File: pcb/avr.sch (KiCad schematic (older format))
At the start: 32 parts, among them IC201 MCU-ATMEGA328P-MU_QFN32_, P201 CONNECTOR, P202 CONNECTOR, P203 CONNECTOR, P204 CONNECTOR, P205 CONNECTOR, P206 CONNECTOR, P207 CONNECTOR, P208 CONNECTOR, P209 CONNECTOR, P210 CONNECTOR, P211 CONNECTOR, P212 CONNECTOR, P213 CONNECTOR, P214 CONNECTOR, P215 CONNECTOR, P216 CONNECTOR, P217 CONNECTOR, P218 CONNECTOR, P219 CONNECTOR, P220 CONNECTOR, P221 CONNECTOR, P222 CONN_01X03, P223 CONNECTOR, P224 CONNECTOR, x201 SMD-CRYSTAL-16MHZ-8PF-20PPM-4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

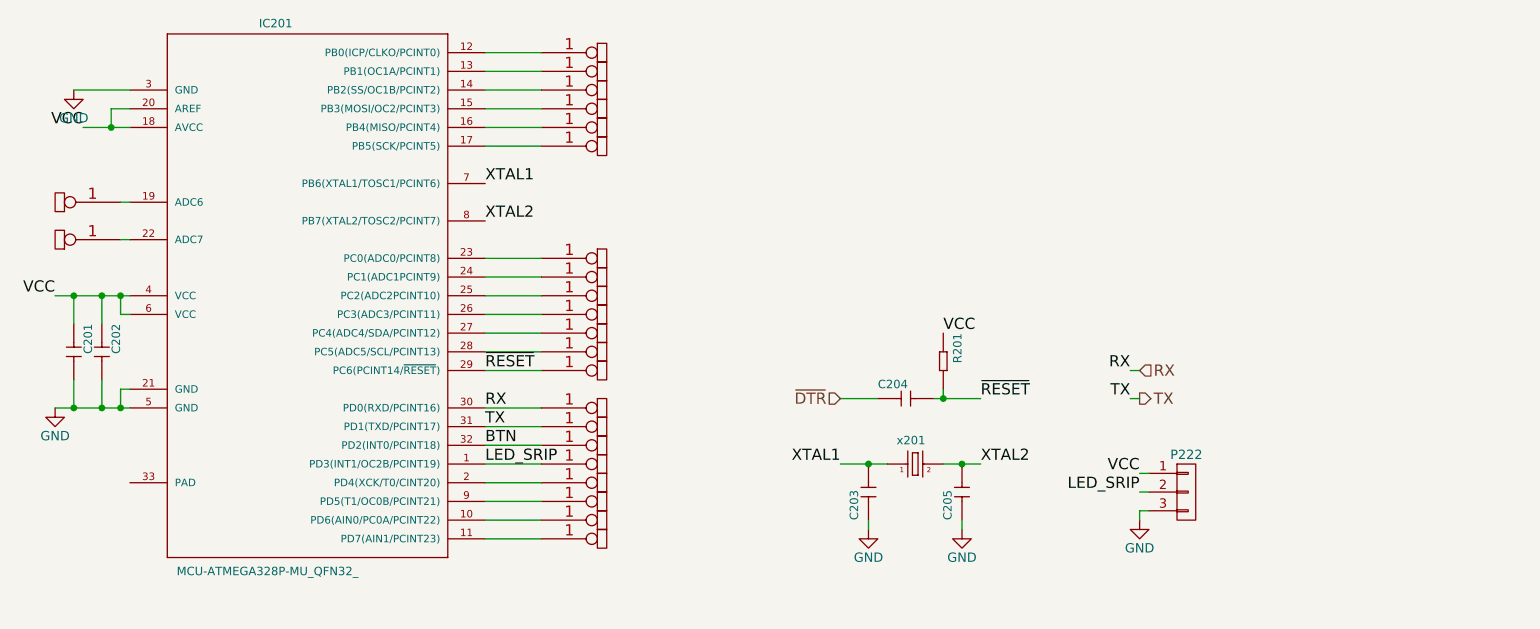
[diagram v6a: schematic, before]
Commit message: added spi header for avr
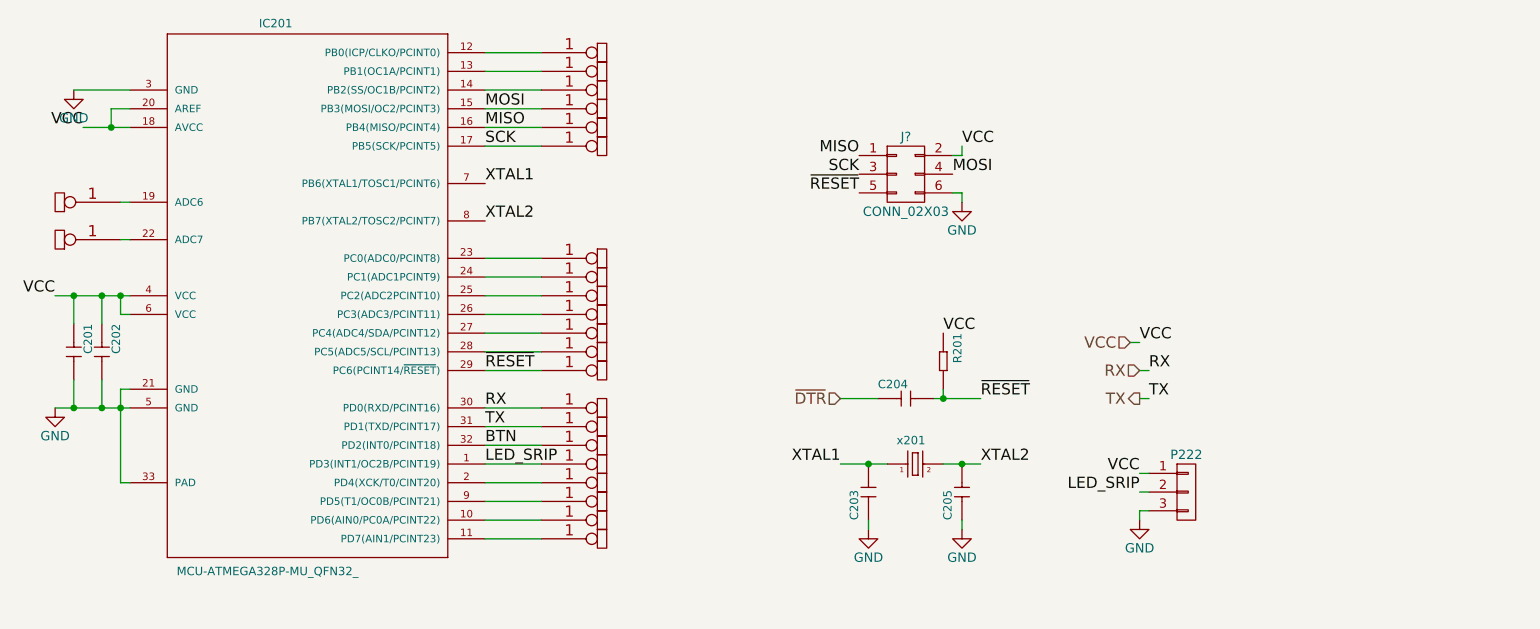
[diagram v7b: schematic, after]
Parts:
- added J?: CONN_02X03, symbol CONN_02X03
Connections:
- net GND: now also IC201.33 (PAD), J?.6 (P6)
- net VCC: now also J?.2 (P2)
- net ~RESET: now also J?.5 (P5)
- net MOSI: now reaches IC201.15 (PB3(MOSI/OC2/PCINT3)), P204.1 (W)
- net MOSI: now also J?.4 (P4)
- net MISO: now reaches IC201.16 (PB4(MISO/PCINT4)), P205.1 (W)
- net MISO: now also J?.1 (P1)
- net SCK: now reaches IC201.17 (PB5(SCK/PCINT5)), P206.1 (W)
- net SCK: now also J?.3 (P3)
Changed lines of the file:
@@
 	1    0    0    -1
 $EndComp
-Wire Wire Line
-	8950 4600 8900 4600
-Wire Wire Line
-	8900 4600 8900 4650
 Text Label 8900 4500 2    60   ~ 0
 LED_SRIP
-Wire Wire Line
-	8950 4500 8900 4500
 Text Label 8900 4400 2    60   ~ 0
 VCC
-Wire Wire Line
-	8950 4400 8900 4400
 $Comp
 L CONNECTOR P223
@@
 	0    1    1    0
 $EndComp
-Wire Wire Line
-	7300 4350 7550 4350
-Wire Wire Line
-	7850 4350 8050 4350
 $Comp
 L GND #PWR09
@@
 	1    0    0    -1
 $EndComp
-Wire Wire Line
-	7450 4650 7450 4700
-Wire Wire Line
-	7950 4650 7950 4700
-Connection ~ 7450 4350
 Text Label 7300 4350 2    60   ~ 0
 XTAL1
 Text Label 8050 4350 0    60   ~ 0
 XTAL2
-Connection ~ 7950 4350
 $Comp
 L CERAMIC-100NF-50V-10%-X7R_0603_ C201
@@
 	1    0    0    -1
 $EndComp
-Wire Wire Line
-	3100 3450 3500 3450
-Wire Wire Line
-	3200 3600 3200 3450
-Connection ~ 3200 3450
-Wire Wire Line
-	3350 3600 3350 3450
-Connection ~ 3350 3450
-Wire Wire Line
-	3500 3550 3450 3550
-Wire Wire Line
-	3450 3550 3450 3450
-Connection ~ 3450 3450
-Wire Wire Line
-	3100 4050 3500 4050
-Wire Wire Line
-	3200 3900 3200 4050
-Connection ~ 3200 4050
-Wire Wire Line
-	3350 3900 3350 4050
-Connection ~ 3350 4050
-Wire Wire Line
-	3500 3950 3450 3950
-Wire Wire Line
-	3450 3950 3450 4050
-Connection ~ 3450 4050
 $Comp
 L GND #PWR012
@@
 Text Label 3250 2550 2    60   ~ 0
 VCC
-Wire Wire Line
-	3250 2550 3500 2550
-Wire Wire Line
-	3500 2350 3200 2350
-Wire Wire Line
-	3500 2450 3400 2450
-Wire Wire Line
-	3400 2450 3400 2550
-Connection ~ 3400 2550
 Text Label 5400 2850 0    60   ~ 0
 XTAL1
 Text Label 5400 3050 0    60   ~ 0
 XTAL2
-Text HLabel 8900 3850 2    60   Input ~ 0
+Text HLabel 8900 3850 0    60   Input ~ 0
 RX
-Text HLabel 8900 4000 2    60   Output ~ 0
+Text HLabel 8900 4000 0    60   Output ~ 0
 TX
-Wire Wire Line
-	5400 4050 5700 4050
-Wire Wire Line
-	5400 4150 5700 4150
 Text Label 5400 4250 0    60   ~ 0
 BTN
@@
 	1    0    0    -1
 $EndComp
-Wire Wire Line
-	7850 3950 7850 4000
-Wire Wire Line
-	7800 4000 8050 4000
-Connection ~ 7850 4000
 Text Label 8050 4000 0    60   ~ 0
 ~RESET
 Text HLabel 7300 4000 0    60   Input ~ 0
 ~DTR
-Wire Wire Line
-	7500 4000 7300 4000
 Text Label 7850 3650 0    60   ~ 0
 VCC
-Wire Wire Line
-	5700 4250 5400 4250
-Wire Wire Line
-	5400 4350 5700 4350
-Wire Wire Line
-	5700 4450 5400 4450
-Wire Wire Line
-	5400 4550 5700 4550
-Wire Wire Line
-	5700 4650 5400 4650
-Wire Wire Line
-	5400 4750 5700 4750
-Wire Wire Line
-	5400 3850 5700 3850
-Wire Wire Line
-	5400 3750 5700 3750
-Wire Wire Line
-	5700 3650 5400 3650
-Wire Wire Line
-	5400 3550 5700 3550
-Wire Wire Line
-	5700 3450 5400 3450
-Wire Wire Line
-	5400 3350 5700 3350
-Wire Wire Line
-	5700 3250 5400 3250
-Wire Wire Line
-	5400 2650 5700 2650
-Wire Wire Line
-	5700 2550 5400 2550
-Wire Wire Line
-	5400 2450 5700 2450
-Wire Wire Line
-	5700 2350 5400 2350
-Wire Wire Line
-	5400 2250 5700 2250
-Wire Wire Line
-	5700 2150 5400 2150
-Wire Wire Line
-	3500 2950 3450 2950
-Wire Wire Line
-	3450 3150 3500 3150
 Text Label 5400 4050 0    60   ~ 0
 RX
 Text Label 5400 4150 0    60   ~ 0
 TX
-Text Label 8850 4000 2    60   ~ 0
+Text Label 8950 4000 0    60   ~ 0
 TX
-Text Label 8850 3850 2    60   ~ 0
+Text Label 8950 3850 0    60   ~ 0
 RX
-Wire Wire Line
-	8900 3850 8850 3850
-Wire Wire Line
-	8900 4000 8850 4000
+$Comp
+L CONN_02X03 J?
+U 1 1 5A551BF4
+P 7650 2800
+F 0 "J?" H 7650 3000 50  0000 C CNN
+F 1 "CONN_02X03" H 7650 2600 50  0000 C CNN
+F 2 "" H 7650 1600 50  0001 C CNN
+F 3 "" H 7650 1600 50  0001 C CNN
+	1    7650 2800
+	1    0    0    -1
+$EndComp
+Text Label 7400 2900 2    60   ~ 0
+~RESET
+Wire Wire Line
+	8950 4600 8900 4600
+Wire Wire Line
+	8900 4600 8900 4650
+Wire Wire Line
+	8950 4500 8900 4500
+Wire Wire Line
+	8950 4400 8900 4400
+Wire Wire Line
+	7300 4350 7450 4350
+Wire Wire Line
+	7450 4350 7550 4350
+Wire Wire Line
+	7850 4350 7950 4350
+Wire Wire Line
+	7950 4350 8050 4350
+Wire Wire Line
+	7450 4650 7450 4700
+Wire Wire Line
+	7950 4650 7950 4700
+Connection ~ 7450 4350
+Connection ~ 7950 4350
+Wire Wire Line
+	3100 3450 3200 3450
+Wire Wire Line
+	3200 3450 3350 3450
+Wire Wire Line
+	3350 3450 3450 3450
+Wire Wire Line
+	3450 3450 3500 3450
+Wire Wire Line
+	3200 3600 3200 3450
+Connection ~ 3200 3450
+Wire Wire Line
+	3350 3600 3350 3450
+Connection ~ 3350 3450
+Wire Wire Line
+	3500 3550 3450 3550
+Wire Wire Line
+	3450 3550 3450 3450
+Connection ~ 3450 3450
+Wire Wire Line
+	3100 4050 3200 4050
+Wire Wire Line
+	3200 4050 3350 4050
+Wire Wire Line
+	3350 4050 3450 4050
+Wire Wire Line
+	3450 4050 3500 4050
+Wire Wire Line
+	3200 3900 3200 4050
+Connection ~ 3200 4050
+Wire Wire Line
+	3350 3900 3350 4050
+Connection ~ 3350 4050
+Wire Wire Line
+	3500 3950 3450 3950
+Wire Wire Line
+	3450 3950 3450 4050
+Wire Wire Line
+	3450 4050 3450 4450
+Connection ~ 3450 4050
+Wire Wire Line
+	3250 2550 3400 2550
+Wire Wire Line
+	3400 2550 3500 2550
+Wire Wire Line
+	3500 2350 3200 2350
+Wire Wire Line
+	3500 2450 3400 2450
+Wire Wire Line
+	3400 2450 3400 2550
+Connection ~ 3400 2550
+Wire Wire Line
+	5400 4050 5700 4050
+Wire Wire Line
+	5400 4150 5700 4150
+Wire Wire Line
+	7850 3950 7850 4000
+Wire Wire Line
+	7800 4000 7850 4000
+Wire Wire Line
+	7850 4000 8050 4000
+Connection ~ 7850 4000
+Wire Wire Line
+	7500 4000 7300 4000
+Wire Wire Line
+	5700 4250 5400 4250
+Wire Wire Line
+	5400 4350 5700 4350
+Wire Wire Line
+	5700 4450 5400 4450
+Wire Wire Line
+	5400 4550 5700 4550
+Wire Wire Line
+	5700 4650 5400 4650
+Wire Wire Line
+	5400 4750 5700 4750
+Wire Wire Line
+	5400 3850 5700 3850
+Wire Wire Line
+	5400 3750 5700 3750
+Wire Wire Line
+	5700 3650 5400 3650
+Wire Wire Line
+	5400 3550 5700 3550
+Wire Wire Line
+	5700 3450 5400 3450
+Wire Wire Line
+	5400 3350 5700 3350
+Wire Wire Line
+	5700 3250 5400 3250
+Wire Wire Line
+	5400 2650 5700 2650
+Wire Wire Line
+	5700 2550 5400 2550
+Wire Wire Line
+	5400 2450 5700 2450
+Wire Wire Line
+	5700 2350 5400 2350
+Wire Wire Line
+	5400 2250 5700 2250
+Wire Wire Line
+	5700 2150 5400 2150
+Wire Wire Line
+	3500 2950 3450 2950
+Wire Wire Line
+	3450 3150 3500 3150
+Wire Wire Line
+	8900 3850 8950 3850
+Wire Wire Line
+	8900 4000 8950 4000
+Wire Wire Line
+	3450 4450 3500 4450
+Text Label 5400 2550 0    60   ~ 0
+MISO
+Text Label 5400 2650 0    60   ~ 0
+SCK
+Text Label 5400 2450 0    60   ~ 0
+MOSI
+Text Label 7900 2800 0    60   ~ 0
+MOSI
+Text Label 7400 2700 2    60   ~ 0
+MISO
+Text Label 7400 2800 2    60   ~ 0
+SCK
+$Comp
+L GND #PWR?
+U 1 1 5A551E4E
+P 7950 2950
+F 0 "#PWR?" H 7950 2700 50  0001 C CNN
+F 1 "GND" H 7950 2800 50  0000 C CNN
+F 2 "" H 7950 2950 50  0000 C CNN
+F 3 "" H 7950 2950 50  0000 C CNN
+	1    7950 2950
+	1    0    0    -1
+$EndComp
+Wire Wire Line
+	7950 2950 7950 2900
+Wire Wire Line
+	7950 2900 7900 2900
+Text Label 7950 2650 0    60   ~ 0
+VCC
+Wire Wire Line
+	7950 2650 7950 2700
+Wire Wire Line
+	7950 2700 7900 2700
+Text HLabel 8850 3700 0    60   Input ~ 0
+VCC
+Text Label 8900 3700 0    60   ~ 0
+VCC
+Wire Wire Line
+	8850 3700 8900 3700
 $EndSCHEMATC

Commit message: finished swapping parts, started layout
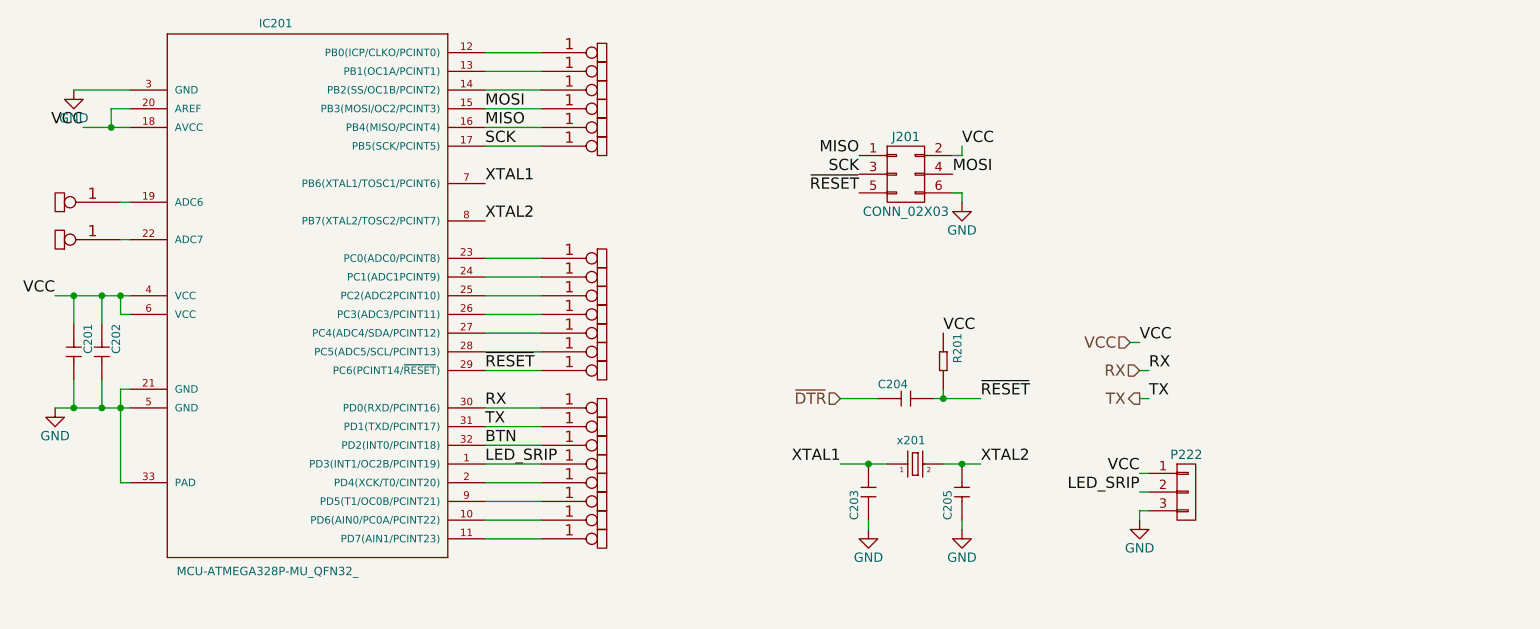
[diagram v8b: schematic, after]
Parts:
- gave numbers to parts that had none: 1
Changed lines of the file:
@@
 $EndComp
 $Comp
-L GND #PWR08
+L GND #PWR05
 U 1 1 58BAB3DE
 P 8900 4650
-F 0 "#PWR08" H 8900 4400 50  0001 C CNN
+F 0 "#PWR05" H 8900 4400 50  0001 C CNN
 F 1 "GND" H 8900 4500 50  0000 C CNN
 F 2 "" H 8900 4650 50  0000 C CNN
@@
 $EndComp
 $Comp
-L GND #PWR09
+L GND #PWR06
 U 1 1 5A3AC4B3
 P 7950 4700
-F 0 "#PWR09" H 7950 4450 50  0001 C CNN
+F 0 "#PWR06" H 7950 4450 50  0001 C CNN
 F 1 "GND" H 7950 4550 50  0000 C CNN
 F 2 "" H 7950 4700 50  0000 C CNN
@@
 $EndComp
 $Comp
-L GND #PWR010
+L GND #PWR07
 U 1 1 5A3AC530
 P 7450 4700
-F 0 "#PWR010" H 7450 4450 50  0001 C CNN
+F 0 "#PWR07" H 7450 4450 50  0001 C CNN
 F 1 "GND" H 7450 4550 50  0000 C CNN
 F 2 "" H 7450 4700 50  0000 C CNN
@@
 $EndComp
 $Comp
-L GND #PWR011
+L GND #PWR08
 U 1 1 5A3AD1F6
 P 3100 4050
-F 0 "#PWR011" H 3100 3800 50  0001 C CNN
+F 0 "#PWR08" H 3100 3800 50  0001 C CNN
 F 1 "GND" H 3100 3900 50  0000 C CNN
 F 2 "" H 3100 4050 50  0001 C CNN
@@
 $EndComp
 $Comp
-L GND #PWR012
+L GND #PWR09
 U 1 1 5A3AE5DA
 P 3200 2350
-F 0 "#PWR012" H 3200 2100 50  0001 C CNN
+F 0 "#PWR09" H 3200 2100 50  0001 C CNN
 F 1 "GND" H 3200 2200 50  0000 C CNN
 F 2 "" H 3200 2350 50  0001 C CNN
@@
 RX
 $Comp
-L CONN_02X03 J?
+L CONN_02X03 J201
 U 1 1 5A551BF4
 P 7650 2800
-F 0 "J?" H 7650 3000 50  0000 C CNN
+F 0 "J201" H 7650 3000 50  0000 C CNN
 F 1 "CONN_02X03" H 7650 2600 50  0000 C CNN
 F 2 "" H 7650 1600 50  0001 C CNN
@@
 	8950 4400 8900 4400
 Wire Wire Line
-	7300 4350 7450 4350
-Wire Wire Line
-	7450 4350 7550 4350
-Wire Wire Line
-	7850 4350 7950 4350
-Wire Wire Line
-	7950 4350 8050 4350
+	7300 4350 7550 4350
+Wire Wire Line
+	7850 4350 8050 4350
 Wire Wire Line
 	7450 4650 7450 4700
@@
 Connection ~ 7950 4350
 Wire Wire Line
-	3100 3450 3200 3450
-Wire Wire Line
-	3200 3450 3350 3450
-Wire Wire Line
-	3350 3450 3450 3450
-Wire Wire Line
-	3450 3450 3500 3450
+	3100 3450 3500 3450
 Wire Wire Line
 	3200 3600 3200 3450
@@
 Connection ~ 3450 3450
 Wire Wire Line
-	3100 4050 3200 4050
-Wire Wire Line
-	3200 4050 3350 4050
-Wire Wire Line
-	3350 4050 3450 4050
-Wire Wire Line
-	3450 4050 3500 4050
+	3100 4050 3500 4050
 Wire Wire Line
 	3200 3900 3200 4050
@@
 	3500 3950 3450 3950
 Wire Wire Line
-	3450 3950 3450 4050
-Wire Wire Line
-	3450 4050 3450 4450
+	3450 3950 3450 4450
 Connection ~ 3450 4050
 Wire Wire Line
-	3250 2550 3400 2550
-Wire Wire Line
-	3400 2550 3500 2550
+	3250 2550 3500 2550
 Wire Wire Line
 	3500 2350 3200 2350
@@
 	7850 3950 7850 4000
 Wire Wire Line
-	7800 4000 7850 4000
-Wire Wire Line
-	7850 4000 8050 4000
+	7800 4000 8050 4000
 Connection ~ 7850 4000
 Wire Wire Line
@@
 SCK
 $Comp
-L GND #PWR?
+L GND #PWR010
 U 1 1 5A551E4E
 P 7950 2950
-F 0 "#PWR?" H 7950 2700 50  0001 C CNN
+F 0 "#PWR010" H 7950 2700 50  0001 C CNN
 F 1 "GND" H 7950 2800 50  0000 C CNN
 F 2 "" H 7950 2950 50  0000 C CNN
